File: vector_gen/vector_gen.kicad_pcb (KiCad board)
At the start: 2 copper layers, 96 parts, among them J1 ARDUINO POWER 3.3V, J10 ARDUINO J1, J11 Conn_01x08, J2 ARDUINO J3 3.3V, J3 ARDUINO J2 3.3V, J5 ARDUINO J1 3.3V, J6 Conn_01x03, J7 ARDUINO POWER, J8 ARDUINO J3, J9 ARDUINO J2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

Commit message: Snapshot of work in progress pcb.
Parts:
- removed C8: 1u, Capacitor_THT:C_Disc_D5.0mm_W2.5mm_P2.50mm
- added C3: 1u, Capacitor_THT:C_Disc_D5.0mm_W2.5mm_P2.50mm, F.Cu at (-54.6, -45.1)
- added C4: 1u, Capacitor_THT:C_Disc_D5.0mm_W2.5mm_P2.50mm, F.Cu at (38.7, -19.7)
- added C5: 1u, Capacitor_THT:C_Disc_D5.0mm_W2.5mm_P2.50mm, F.Cu at (26.7, 10.2)
- moved R20 110.0 mm to (18.4, -0.64), turned to 90 degrees
- moved R25 79.6 mm to (30.5, -10.2)
- moved C20 74.5 mm to (-55.2, 7.62), turned to 90 degrees
- moved J6 74.5 mm to (49.5, -41.3), turned to 270 degrees
- moved R23 70.3 mm to (24.8, -10.8), turned to 270 degrees
- moved C7 67.6 mm to (-30.5, -45.1), turned to 90 degrees
- moved R14 66.0 mm to (-7.62, -27.9)
- moved TP7 63.3 mm to (8.26, -32.4)
- moved TP6 61.3 mm to (-52.1, -30.5)
- moved TP18 60.7 mm to (-41.9, -30.5)
- moved TP17 60.6 mm to (-47.0, -30.5)
- moved R19 60.5 mm to (40.6, -6.35)
- moved U11 59.7 mm to (8.26, 12.7)
- moved TP22 58.8 mm to (-19.1, -30.5)
- moved C15 57.8 mm to (10.8, -41.9)
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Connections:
- R21 pad 1: -5V -> GND
- U5 pad 7: Net-(C10-Pad1) -> GND
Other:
- net class POWER added: clearance 0.2, trace_width 0.499999, via_dia 0.8, via_drill 0.4
- rule via_min_drill: 0.3 -> 0.254
- rule via_min_size: 0.4 -> 0.508

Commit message: PCB almost routed.
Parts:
- removed TP10, TP17, TP18, TP19, TP20, TP21, TP22, TP6, TP7, TP8, TP9: TestPoint, TestPoint:TestPoint_THTPad_2.5x2.5mm_Drill1.2mm
- moved TP1 45.4 mm to (42.5, -31.1)
- moved R3 44.5 mm to (-7.62, 26.7), turned to 90 degrees
- moved TP4 42.3 mm to (-29.8, -47.0)
- moved TP5 40.9 mm to (-26.0, -47.0)
- moved R28 40.4 mm to (-21.0, 16.5)
- moved TP13 36.2 mm to (42.5, -27.3)
- moved TP12 33.8 mm to (42.5, 5.71)
- moved R17 30.4 mm to (27.3, -21.0), turned to 180 degrees
- moved R20 29.1 mm to (35.6, -24.1), turned to 180 degrees
- moved R16 28.0 mm to (-34.3, 16.5)
- moved J11 26.5 mm to (-34.3, -31.8), turned to 270 degrees
- moved R24 23.8 mm to (34.3, -10.8), turned to 90 degrees
- moved U10 21.0 mm to (-1.27, -15.2)
- moved C1 20.5 mm to (-52.7, -14.0), turned to 0 degrees
- moved R27 19.8 mm to (14.0, 0.00)
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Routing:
- net +5V: track 0.00 -> 428.3 mm
- net Net-(J11-Pad7): track 0.00 -> 218.9 mm
- net Net-(J8-Pad6): track 0.00 -> 131.0 mm
- net Net-(J9-Pad3): track 0.00 -> 106.3 mm
- net Net-(C12-Pad1): track 0.00 -> 100.5 mm
- net Net-(J10-Pad8): track 0.00 -> 94.5 mm
- net Net-(J9-Pad2): track 0.00 -> 91.5 mm
- net Net-(J9-Pad1): track 0.00 -> 83.9 mm
- net Net-(J8-Pad4): track 0.00 -> 81.1 mm
- net Net-(J10-Pad4): track 0.00 -> 80.2 mm
- net Net-(J11-Pad4): track 0.00 -> 79.0 mm
- net Net-(C11-Pad1): track 0.00 -> 77.7 mm
- net Net-(J11-Pad3): track 0.00 -> 66.9 mm
- net Net-(J9-Pad4): track 0.00 -> 65.7 mm
- net -5V: track 0.00 -> 60.6 mm
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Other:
- board outline added: 108.6 x 83.2 mm
- board text added: "+5V"
- board text added: "-5V"
- board text added: "3.3V"
- board text added: "GND"
- board text added: "Male pins on bottom plug into MCU board (Arduino Uno pinout)"
- board text removed: "The connectors are flipped because the MCU board will be plugged in top down"

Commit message: More routing.
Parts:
- added J4: Conn_01x02_Female, Connector_PinHeader_2.54mm:PinHeader_1x02_P2.54mm_Vertical, F.Cu at (8.26, 1.91)
- moved TP15 63.6 mm to (4.45, 8.89)
- moved TP14 57.8 mm to (4.45, 5.08)
- moved R27 9.53 mm to (4.45, 0.00)
- moved R23 6.38 mm to (17.1, 1.91)
- moved R29 2.01 mm to (0.00, 12.7)
- moved R30 1.91 mm to (-3.81, 12.7)
- moved R26 1.42 mm to (-5.71, -5.08)
- moved TP16 1.42 mm to (-10.8, -15.9)
- moved RN2 1.27 mm to (-15.2, -15.9)
- moved R20 0.64 mm to (34.9, -24.1)
- moved R5 0.63 mm to (-21.0, -31.8)
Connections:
- TP14 pad 1: Net-(J11-Pad5) -> Net-(J4-Pad1)
- TP15 pad 1: Net-(J11-Pad6) -> Net-(J4-Pad2)
- U11 pad 10: Net-(J11-Pad6) -> Net-(J4-Pad2)
- U11 pad 14: Net-(J11-Pad5) -> Net-(J4-Pad1)
- U9 pad 10: Net-(J11-Pad6) -> Net-(J4-Pad2)
- U9 pad 5: Net-(J11-Pad5) -> Net-(J4-Pad1)
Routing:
- net Net-(J8-Pad4): track 81.1 -> 150.9 mm, vias 0 -> 1
- net Net-(J10-Pad3): track 4.45 -> 73.4 mm, vias 0 -> 1
- net Net-(J5-Pad4): track 0.00 -> 58.0 mm, vias 0 -> 1
- net Net-(TP16-Pad1): track 6.02 -> 54.8 mm, vias 0 -> 1
- net Net-(J4-Pad2): track 0.00 -> 39.6 mm
- net Net-(R16-Pad2): track 0.00 -> 31.7 mm
- net Net-(R27-Pad1): track 0.00 -> 31.2 mm
- net Net-(J10-Pad7): track 28.8 -> 57.3 mm, vias 0 -> 1
- net -5V: track 60.6 -> 87.4 mm
- net Net-(J11-Pad6): track 23.0 -> 0.00 mm
- net Net-(J11-Pad5): track 12.5 -> 0.00 mm
- net Net-(J4-Pad1): track 0.00 -> 12.3 mm
- net +5V: track 428.3 -> 424.3 mm
- net Net-(J2-Pad1): track 0.00 -> 3.81 mm
- net Net-(J8-Pad6): track 131.0 -> 134.5 mm
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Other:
- board text added: "INTENSITY"
- board text added: "Male pins on bottom plug into MCU board (Arduino Uno pinout). Install for 3.3V or 5V"
- board text added: "Vector generator Copyright (C) 2022 toby@telegraphics.com.au"
- board text added: "X"
- board text added: "Y"
- board text added: "Z"
- board text removed: "Male pins on bottom plug into MCU board (Arduino Uno pinout)"

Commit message: Rerrange layout
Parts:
- added H1: MountingHole, MountingHole:MountingHole_3.2mm_M3, F.Cu at (-54.0, -52.1)
- added H2: MountingHole, MountingHole:MountingHole_3.2mm_M3, F.Cu at (27.3, 40.6)
- added H3: MountingHole, MountingHole:MountingHole_3.2mm_M3, F.Cu at (27.3, -52.1)
- added H4: MountingHole, MountingHole:MountingHole_3.2mm_M3, F.Cu at (-54.0, 40.6)
- moved YOUT1 67.3 mm to (3.17, 36.8)
- moved TP13 66.7 mm to (2.54, 26.0)
- moved TP1 64.7 mm to (2.54, 19.7)
- moved Q1 58.9 mm to (-36.2, 37.5), turned to 0 degrees
- moved R21 57.8 mm to (-43.2, 31.1), turned to 0 degrees
- moved RV1 56.5 mm to (-48.3, 31.8), turned to 90 degrees
- moved ZOUT1 55.7 mm to (-10.8, 36.8)
- moved U19 54.1 mm to (-29.2, 39.4)
- moved R1 48.5 mm to (-13.3, -50.8), turned to 0 degrees
- moved XOUT1 47.4 mm to (17.1, 36.8)
- moved TP11 47.2 mm to (-2.54, 26.0)
- moved TP12 40.4 mm to (7.62, 26.0)
- moved R24 38.1 mm to (27.3, 26.7)
- moved J6 33.6 mm to (26.0, -15.2)
- moved U8 32.9 mm to (12.7, 27.9)
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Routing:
- net +5V: track 424.3 -> 497.1 mm
- net Net-(J10-Pad8): track 97.3 -> 42.3 mm
- net Net-(R17-Pad1): track 36.0 -> 74.3 mm
- net Net-(J11-Pad7): track 219.3 -> 198.5 mm
- net Net-(R15-Pad1): track 33.7 -> 49.7 mm
- net Net-(R19-Pad1): track 16.0 -> 30.5 mm
- net Net-(C12-Pad1): track 100.5 -> 114.1 mm
- net Net-(J4-Pad1): track 12.3 -> 25.8 mm
- net -5V: track 87.4 -> 100.1 mm
- net Net-(R11-Pad1): track 6.77 -> 18.2 mm
- net Net-(R22-Pad2): track 9.31 -> 19.6 mm
- net Net-(R25-Pad1): track 37.7 -> 30.5 mm
- net Net-(J8-Pad4): track 150.9 -> 144.3 mm
- net Net-(J11-Pad1): track 32.0 -> 38.0 mm
- net Net-(J11-Pad4): track 78.3 -> 72.6 mm
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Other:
- board size 108.6 x 83.2 mm -> 91.4 x 101.6 mm
- board text added: "Standoffs must be at least 15mm Hole 3mm to match brass 5mm body I have in stock Standoff must have at least 10mm vertical clearance from outer pin centre to not interfere with dev board"

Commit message: Ground plane done?
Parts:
- added D1: LED, LED_THT:LED_D3.0mm, F.Cu at (-50.2, 19.1)
- added R2: 330, Resistor_THT:R_Axial_DIN0207_L6.3mm_D2.5mm_P10.16mm_Horizontal, F.Cu at (-50.2, 36.8)
- moved J4 5.16 mm to (13.3, 1.02)
- moved R23 5.03 mm to (18.9, 1.02)
- moved R27 4.49 mm to (8.89, 0.64)
- moved TP16 1.27 mm to (-10.8, -14.6)
- moved R19 1.14 mm to (29.1, -2.54)
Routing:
- net Net-(J10-Pad8): track 42.3 -> 64.8 mm, vias 0 -> 1
- net Net-(R19-Pad1): track 30.5 -> 51.5 mm
- net Net-(J11-Pad7): track 198.5 -> 219.3 mm
- net GND: track 0.47 -> 18.4 mm
- net Net-(D1-Pad1): track 0.00 -> 17.8 mm
- net -5V: track 100.1 -> 86.5 mm
- net Net-(J9-Pad3): track 107.5 -> 119.4 mm
- net Net-(J10-Pad3): track 73.7 -> 85.2 mm
- net +5V: track 497.1 -> 508.0 mm
- net Net-(J4-Pad1): track 25.8 -> 33.8 mm
- net Net-(R23-Pad2): track 20.0 -> 25.0 mm
- net Net-(R26-Pad1): track 24.1 -> 28.8 mm
- net Net-(J10-Pad4): track 78.4 -> 81.8 mm
- net Net-(C12-Pad1): track 114.1 -> 110.8 mm, vias 0 -> 1
- net Net-(J8-Pad2): track 57.7 -> 60.2 mm
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- added copper zone on B.Cu, net GND

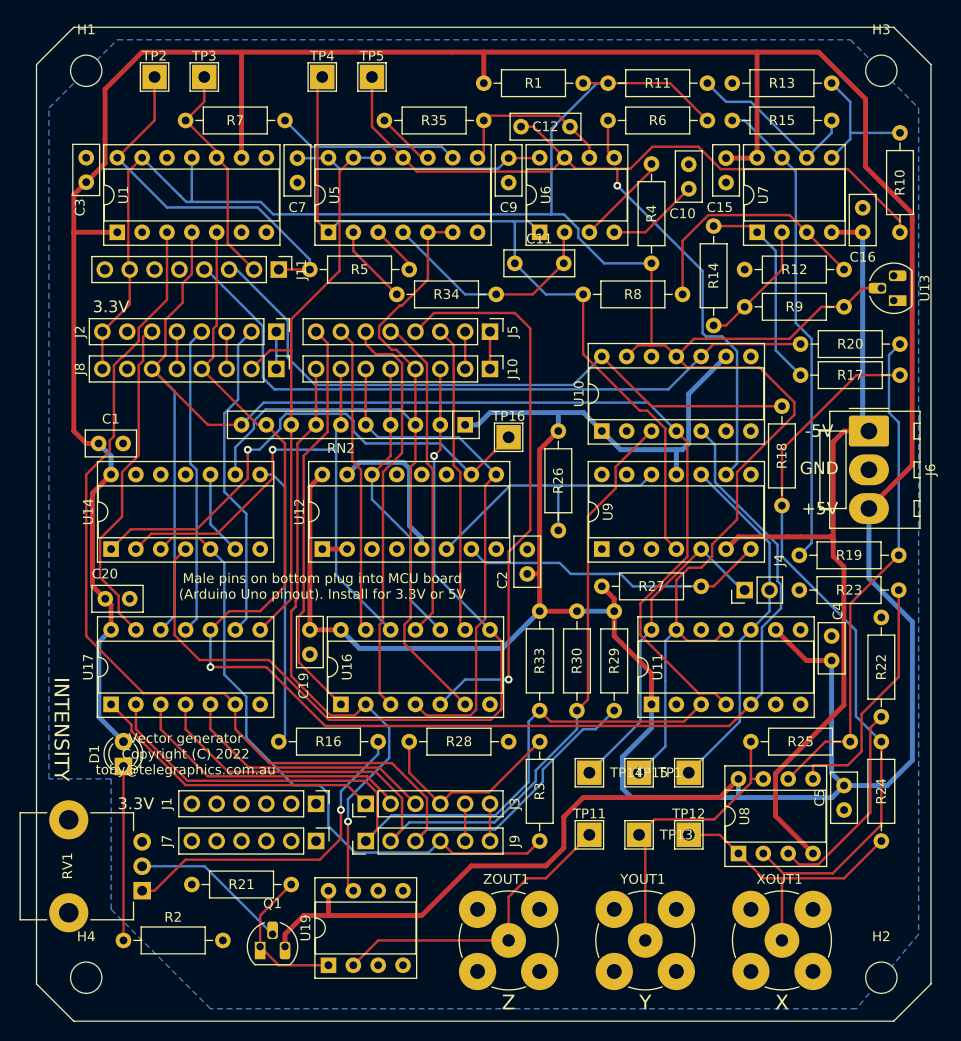
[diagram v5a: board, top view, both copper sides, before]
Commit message: Add fill to front copper and suggestions from joe_z.
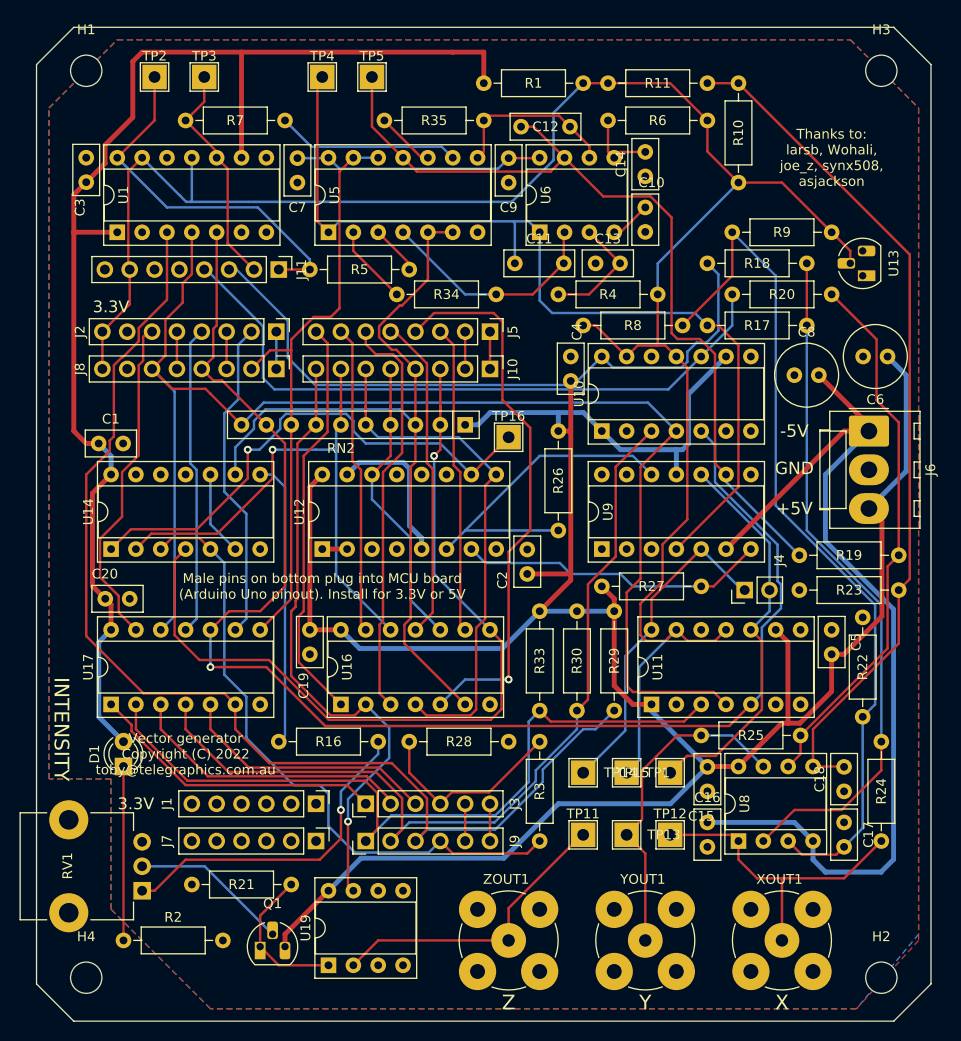
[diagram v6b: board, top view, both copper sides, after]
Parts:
- removed R12, R13, R14, R15: 33k, Resistor_THT:R_Axial_DIN0207_L6.3mm_D2.5mm_P10.16mm_Horizontal
- removed U7: TL072IP, Package_DIP:DIP-8_W7.62mm_Socket
- added C13: .1u, Capacitor_THT:C_Disc_D5.0mm_W2.5mm_P2.50mm, F.Cu at (-1.91, -32.4)
- added C14: .1u, Capacitor_THT:C_Disc_D5.0mm_W2.5mm_P2.50mm, F.Cu at (3.17, -41.3)
- added C17: .1u, Capacitor_THT:C_Disc_D5.0mm_W2.5mm_P2.50mm, F.Cu at (23.5, 24.8)
- added C18: .1u, Capacitor_THT:C_Disc_D5.0mm_W2.5mm_P2.50mm, F.Cu at (23.5, 21.6)
- added C6: 100u, Capacitor_THT:C_Radial_D6.3mm_H7.0mm_P2.50mm, F.Cu at (27.9, -22.9)
- added C8: 100u, Capacitor_THT:C_Radial_D6.3mm_H7.0mm_P2.50mm, F.Cu at (18.4, -21.0)
- R22, R23: value 11k -> 15k
- moved C16 62.4 mm to (9.53, 24.8), turned to 270 degrees
- moved C15 62.3 mm to (9.53, 21.6)
- moved C4 39.1 mm to (-4.45, -22.9)
- moved R18 24.9 mm to (19.7, -32.4), turned to 180 degrees
- moved C5 18.5 mm to (22.2, 5.08), turned to 270 degrees
- moved R10 17.3 mm to (12.7, -50.8)
- moved R4 16.4 mm to (-5.71, -29.2), turned to 0 degrees
- moved R17 10.8 mm to (19.7, -26.0)
- moved R20 8.64 mm to (22.2, -29.2)
- moved R9 7.73 mm to (12.1, -35.6)
- moved R25 5.12 mm to (8.89, 15.9)
- moved C10 4.84 mm to (3.17, -38.1), turned to 270 degrees
- moved U13 4.07 mm to (25.4, -31.1)
- moved R8 3.18 mm to (6.99, -26.0)
- moved R22 1.91 mm to (25.4, 3.81)
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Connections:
- R10 pad 1: Net-(R10-Pad1) -> Net-(C18-Pad2)
- R10 pad 2: Net-(C12-Pad1) -> Net-(J11-Pad7)
- R11 pad 1: Net-(R11-Pad1) -> Net-(C18-Pad2)
- R17 pad 2: Net-(R14-Pad1) -> Net-(C11-Pad1)
- R19 pad 2: Net-(R15-Pad1) -> Net-(C12-Pad1)
- R22 pad 2: Net-(R22-Pad2) -> Net-(C17-Pad2)
- R23 pad 2: Net-(R23-Pad2) -> Net-(C18-Pad2)
- R8 pad 1: Net-(R12-Pad2) -> Net-(C17-Pad2)
- R8 pad 2: Net-(C11-Pad1) -> Net-(J11-Pad7)
- R9 pad 1: Net-(R14-Pad2) -> Net-(C17-Pad2)
- U8 pad 3: Net-(R22-Pad2) -> Net-(C17-Pad2)
- U8 pad 5: Net-(R23-Pad2) -> Net-(C18-Pad2)
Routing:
- net +5V: track 508.0 -> 394.3 mm
- net Net-(C17-Pad2): track 0.00 -> 88.4 mm
- net Net-(C18-Pad2): track 0.00 -> 87.6 mm
- net Net-(R15-Pad1): track 49.1 -> 0.00 mm
- net Net-(R12-Pad2): track 26.0 -> 0.00 mm
- net Net-(R23-Pad2): track 25.0 -> 0.00 mm
- net Net-(C12-Pad1): track 110.8 -> 87.8 mm, vias 1 -> 0
- net Net-(R22-Pad2): track 21.3 -> 0.00 mm
- net Net-(R14-Pad1): track 21.2 -> 0.00 mm
- net Net-(R11-Pad1): track 18.2 -> 0.00 mm
- net Net-(R10-Pad1): track 14.3 -> 0.00 mm
- net Net-(C11-Pad1): track 82.2 -> 96.1 mm
- net Net-(R14-Pad2): track 13.2 -> 0.00 mm
- net -5V: track 86.5 -> 98.8 mm
- net Net-(J11-Pad7): track 219.3 -> 210.2 mm
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- added copper zone on F.Cu, net GND
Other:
- board text added: "In memory of bootnecklad 1995–2018"
- board text added: "Thanks to: larsb, Wohali, joe_z, synx508, asjackson"

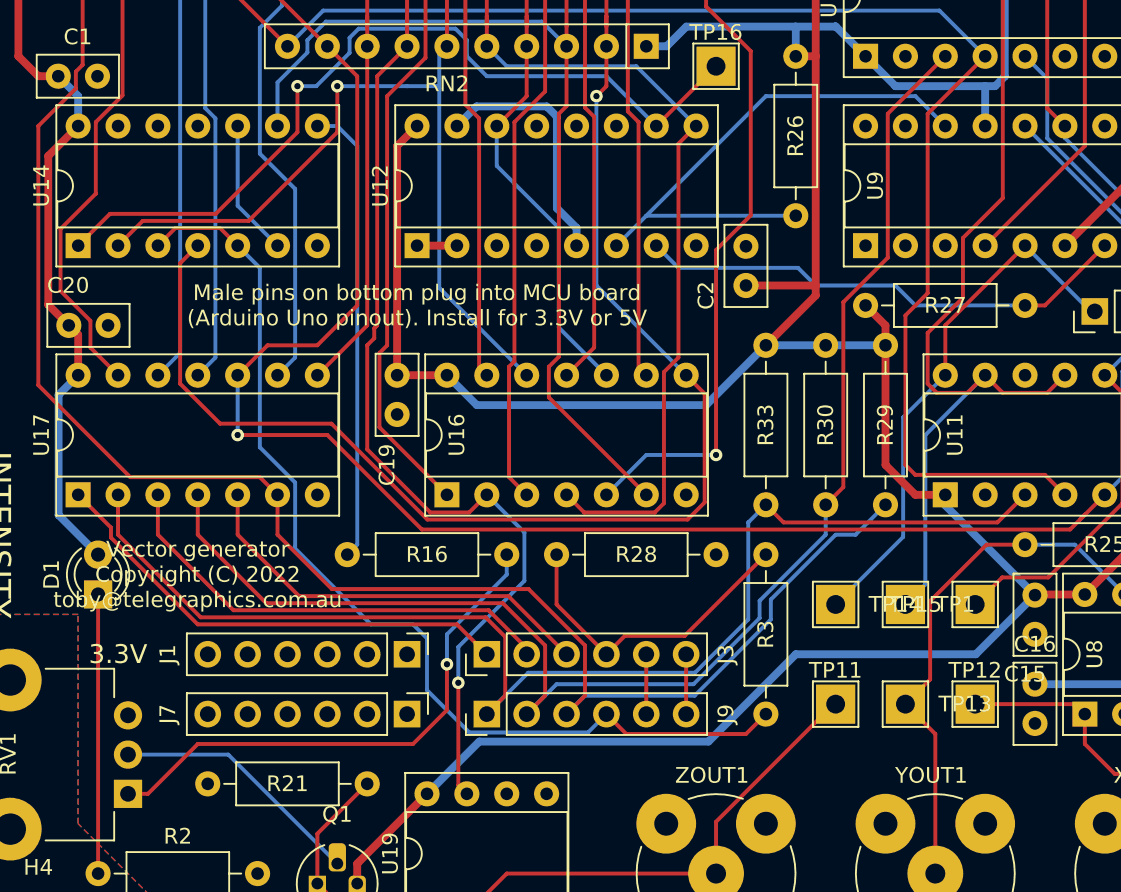
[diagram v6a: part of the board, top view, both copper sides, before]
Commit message: Fix a connectivity issue.
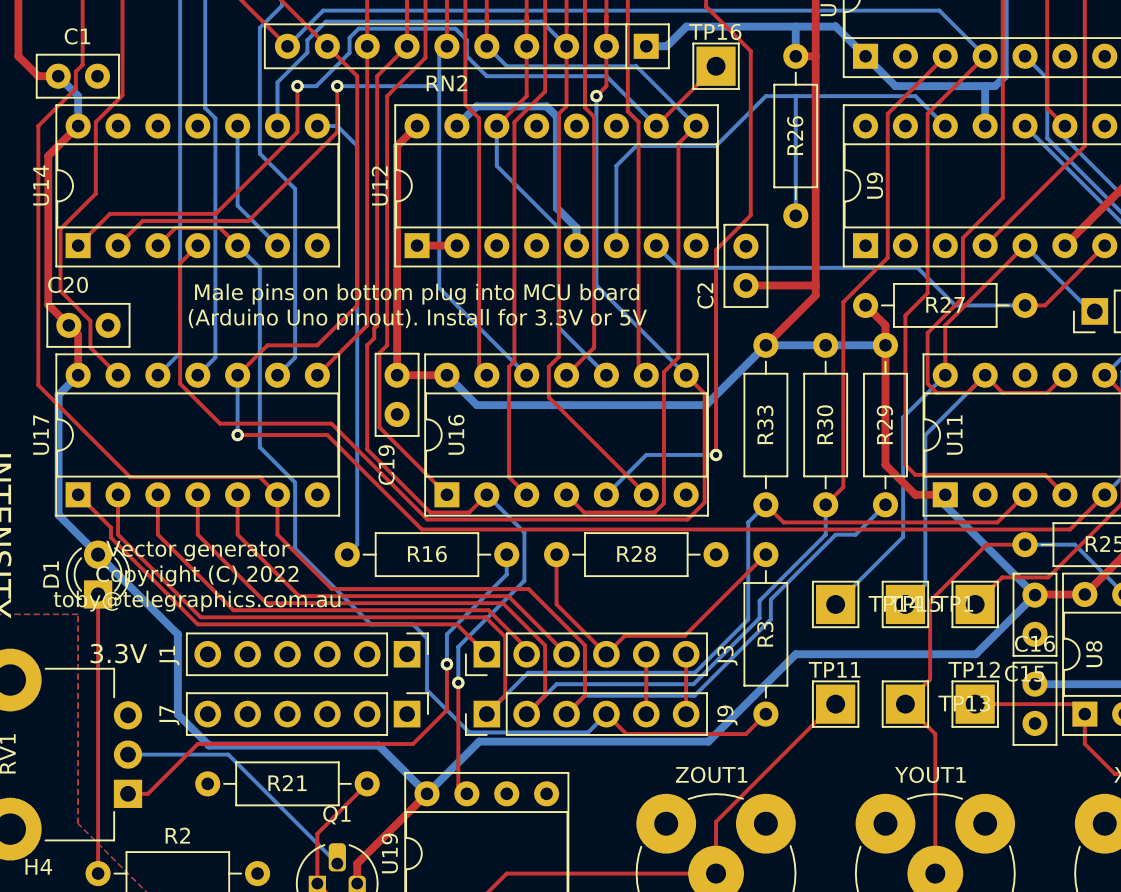
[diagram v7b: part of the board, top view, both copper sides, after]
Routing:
- net +5V: track 394.3 -> 424.6 mm
- net Net-(R26-Pad1): track 35.2 -> 36.3 mm

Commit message: Updated.
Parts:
- added C21: 1u, Capacitor_THT:C_Disc_D5.0mm_W2.5mm_P2.50mm, F.Cu at (17.1, -13.3)
- added C22: 1u, Capacitor_THT:C_Disc_D5.0mm_W2.5mm_P2.50mm, F.Cu at (17.1, -5.08)
- added R12: 100k? to be determined, Resistor_THT:R_Axial_DIN0207_L6.3mm_D2.5mm_P10.16mm_Horizontal, F.Cu at (-5.08, -6.35)
- added R13: 100k? to be determined, Resistor_THT:R_Axial_DIN0207_L6.3mm_D2.5mm_P10.16mm_Horizontal, F.Cu at (0.64, 1.27)
- moved R27 23.5 mm to (-14.6, 0.64), turned to 0 degrees
- moved R26 2.84 mm to (-8.26, -6.35)
- moved C2 2.54 mm to (-8.89, -3.17), turned to 0 degrees
- moved TP16 1.27 mm to (-12.1, -14.6)
- moved C20 0.63 mm to (-50.2, 1.91)
- moved J4 0.25 mm to (13.3, 1.27)
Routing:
- net +5V: track 424.6 -> 467.7 mm
- net -5V: track 98.8 -> 74.0 mm
- net GND: track 18.4 -> 0.00 mm
- net Net-(C11-Pad1): track 96.1 -> 113.8 mm
- net Net-(R12-Pad1): track 36.3 -> 24.1 mm
- net Net-(C12-Pad1): track 87.8 -> 99.2 mm
- net Net-(J10-Pad3): track 85.2 -> 90.9 mm, vias 1 -> 0
- net Net-(J11-Pad7): track 210.2 -> 204.7 mm
- net Net-(J8-Pad6): track 141.1 -> 136.3 mm
- net Net-(R13-Pad1): track 31.7 -> 35.3 mm
- net Net-(C17-Pad2): track 88.4 -> 84.9 mm
- net Net-(J5-Pad4): track 56.8 -> 53.4 mm
- net Net-(R17-Pad1): track 70.0 -> 73.1 mm
- net Net-(J2-Pad6): track 34.4 -> 31.7 mm
- net Net-(J9-Pad4): track 65.2 -> 66.8 mm
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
